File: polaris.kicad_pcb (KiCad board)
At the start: 4 copper layers, 170 parts, among them J1001 Conn_Coaxial, J101 XT60-M, J102 PYRO0, J103 PYRO1, J104 PYRO2, J105 PYRO3, J106 PYRO4, J107 PYRO5, J108 SERVO0, J109 SERVO1, J110 SERVO2, J111 SERVO3, J112 SERVO4, J113 SERVO5, J114 SPI, J115 I2C, J116 PB, J117 SWD, J301 USB_C_Receptacle_USB2.0_16P, J401 GNSS, J501 XT60-M, Q201 IRLZ44N, Q202 IRLZ44N, Q401 Q_NMOS, Q501 IRLZ44N, Q502 IRLZ44N, Q503 IRLZ44N, Q504 IRLZ44N, Q505 IRLZ44N, Q506 IRLZ44N, SW401 SW_Push, SW402 SW_Push, U1001 Ra-08H, U1101 THD-2528-11SD-GF, U1201 W25Q128JVE, U201 BQ24005, U202 LM74700, U203 LM74700, U204 TLV75733PDBV, U205 LMR51430, U206 TPS7A2033PDBVR, U301 USBLC6-2SC6, U302 CH224K, U303 USBLC6-2SC6, U403 STM32F446VETx, U501 PC817, U502 PC817, U503 PC817, U504 PC817, U505 PC817, U506 PC817, U507 CD4051B, U601 ICM-42688-P, U701 LSM6DSO32TR, U801 MS5607, U901 LPS22HH, Y401 YXC YSX321SL

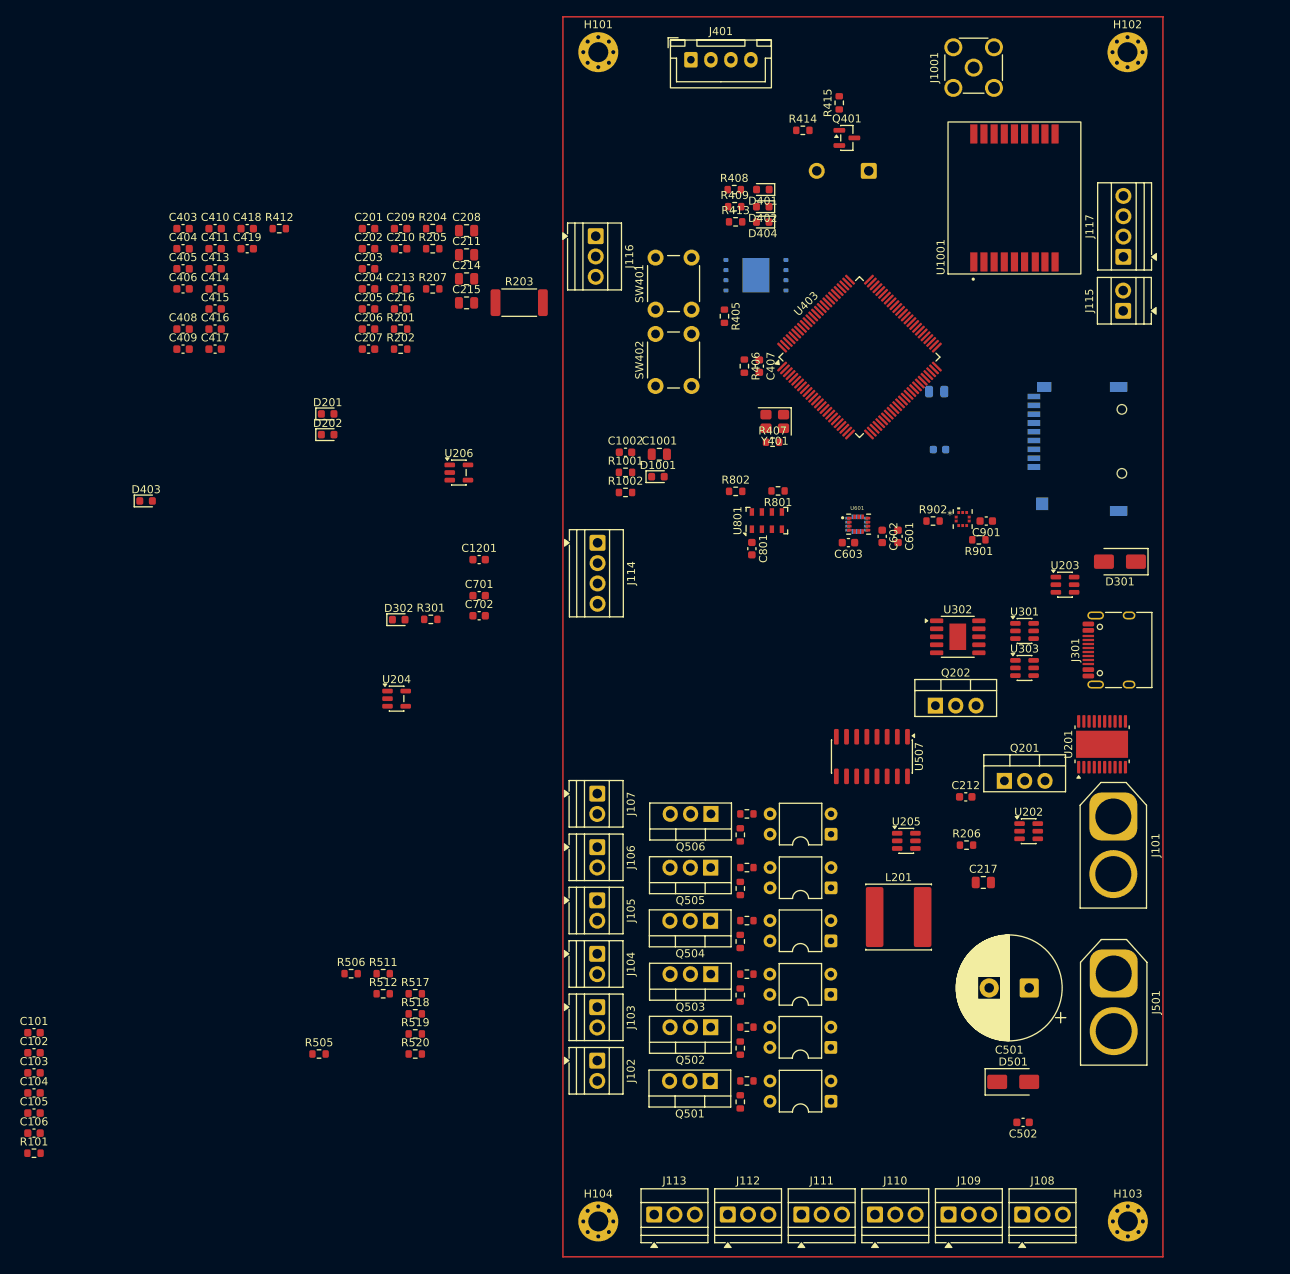
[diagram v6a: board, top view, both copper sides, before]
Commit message: Continued rough component placement
Finished most of component placement, only a few passives remain
Board dimensions basically locked at 155x75 mm
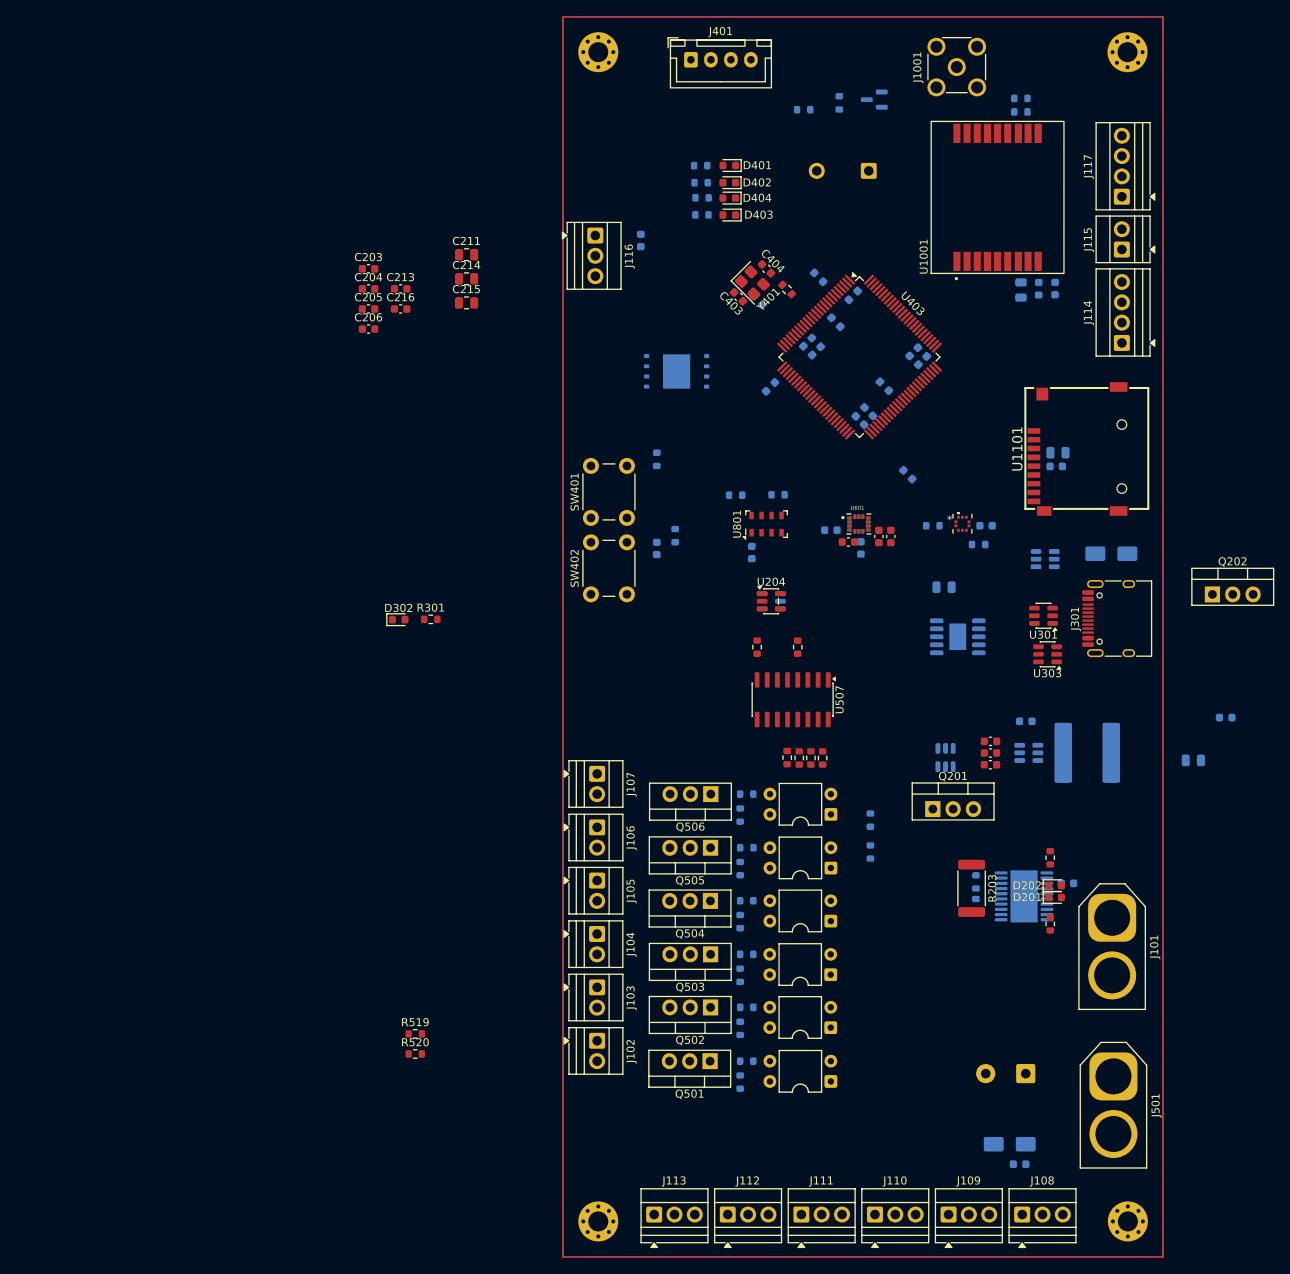
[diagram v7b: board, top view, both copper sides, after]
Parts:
- removed C101, C102, C103, C104, C105, C106: 100n, Capacitor_SMD:C_0603_1608Metric
- removed R101: 0R, Resistor_SMD:R_0603_1608Metric
- C1001, C1002, C1201, C201, C202, C208, C212, C217, C405, C406, C407, C408, C409, C410, C411, C413, C414, C415, C416, C417, C418, C419, C501, C701, C702, C801, C901, D1001, D301, D501, L201, Q401, R1001, R1002, R201, R202, R206, R207, R405, R406, R408, R409, R412, R413, R414, R415, R501, R502, R503, R504, R507, R508, R509, R510, R513, R514, R515, R516, R801, R802, R901, R902, U201, U202, U203, U205, U206, U302: moved to B.Cu
- C502: value C -> 4u7; moved to B.Cu
- U1101: moved to F.Cu
- moved C201 123.3 mm to (169.8, 112.6)
- moved C202 118.0 mm to (150.1, 133.3)
- moved R205 114.4 mm to (147.9, 138.4), turned to -90 degrees
- moved R204 110.2 mm to (147.9, 130.1), turned to 90 degrees
- moved D201 109.2 mm to (148.5, 135.1)
- moved D202 107.0 mm to (148.5, 133.6)
- moved R202 100.1 mm to (138.6, 136.1), turned to -90 degrees
- moved R201 99.7 mm to (138.6, 133.1), turned to -90 degrees
- moved C209 97.7 mm to (140.4, 115.6), turned to 180 degrees
- moved C210 97.0 mm to (140.4, 117.0), turned to 180 degrees
- moved C207 93.5 mm to (140.4, 118.5), turned to 180 degrees
- moved R203 92.5 mm to (138.1, 133.9), turned to -90 degrees
- moved C410 91.9 mm to (130.1, 82.2), turned to -45 degrees
- moved C409 91.4 mm to (130.9, 67.9), turned to 135 degrees
- moved C413 89.0 mm to (131.9, 66.9), turned to 135 degrees
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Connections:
- C405 pad 1: Net-(U403-VREF+) -> +3.3V
- C406 pad 1: Net-(U403-VREF+) -> +3.3V
- C501 pad 2: GND1 -> GND
- C502 pad 2: GND1 -> GND
- D501 pad 1: GND1 -> GND
- J108 pad 3: GND1 -> GND
- J109 pad 3: GND1 -> GND
- J110 pad 3: GND1 -> GND
- J111 pad 3: GND1 -> GND
- J112 pad 3: GND1 -> GND
- J113 pad 3: GND1 -> GND
- U403 pad 21: Net-(U403-VREF+) -> +3.3V
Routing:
- removed copper zone on In1.Cu, net GND
- removed copper zone on In2.Cu, net GND

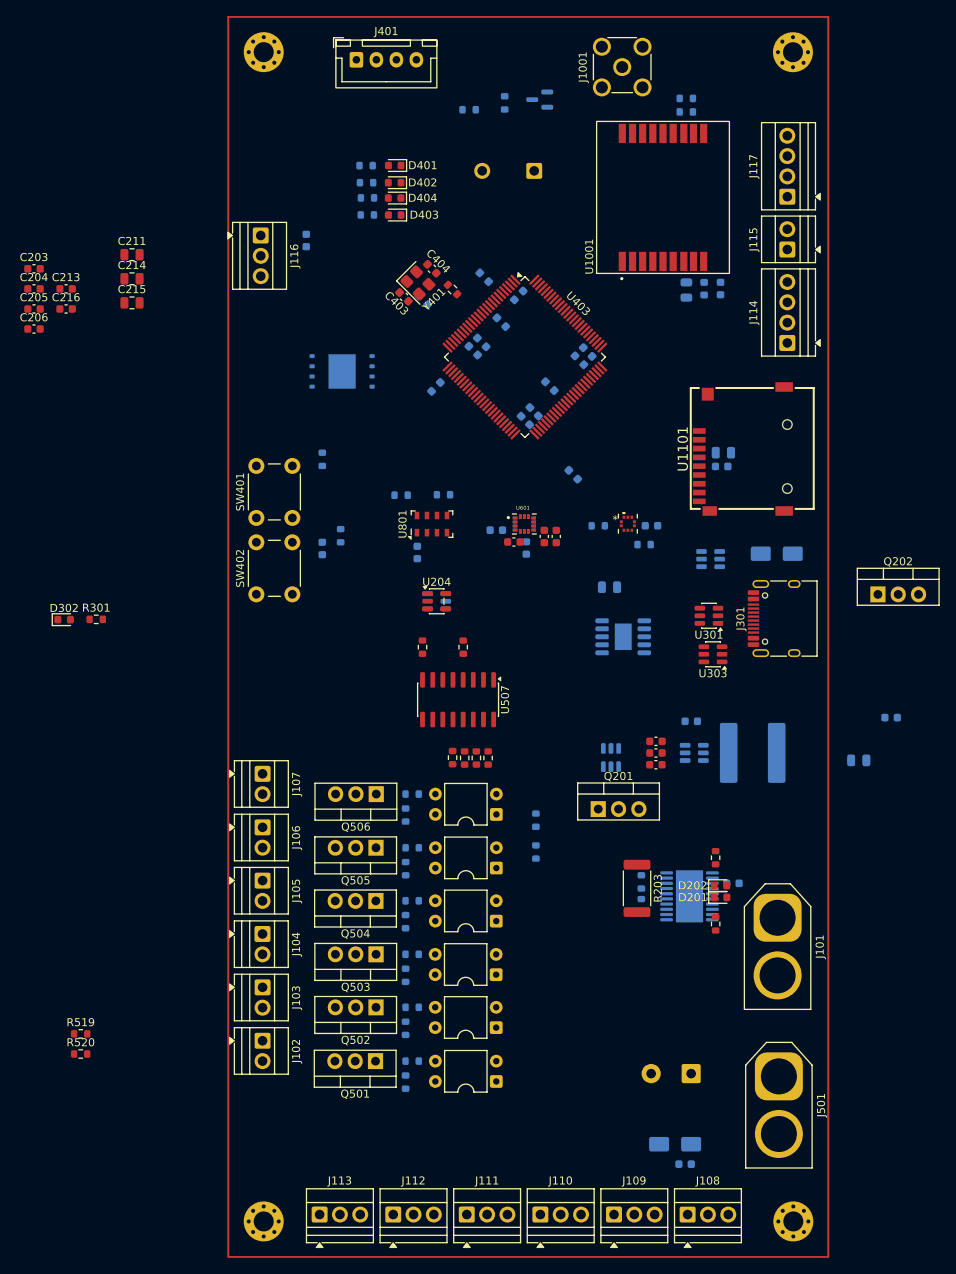
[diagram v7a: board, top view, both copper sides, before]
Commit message: Completed rough component placement
Began laying out traces
Small change to page 12 of schematic (FLASH):
Connected exposed pad to GND (not sure why I didn't connect it previously)
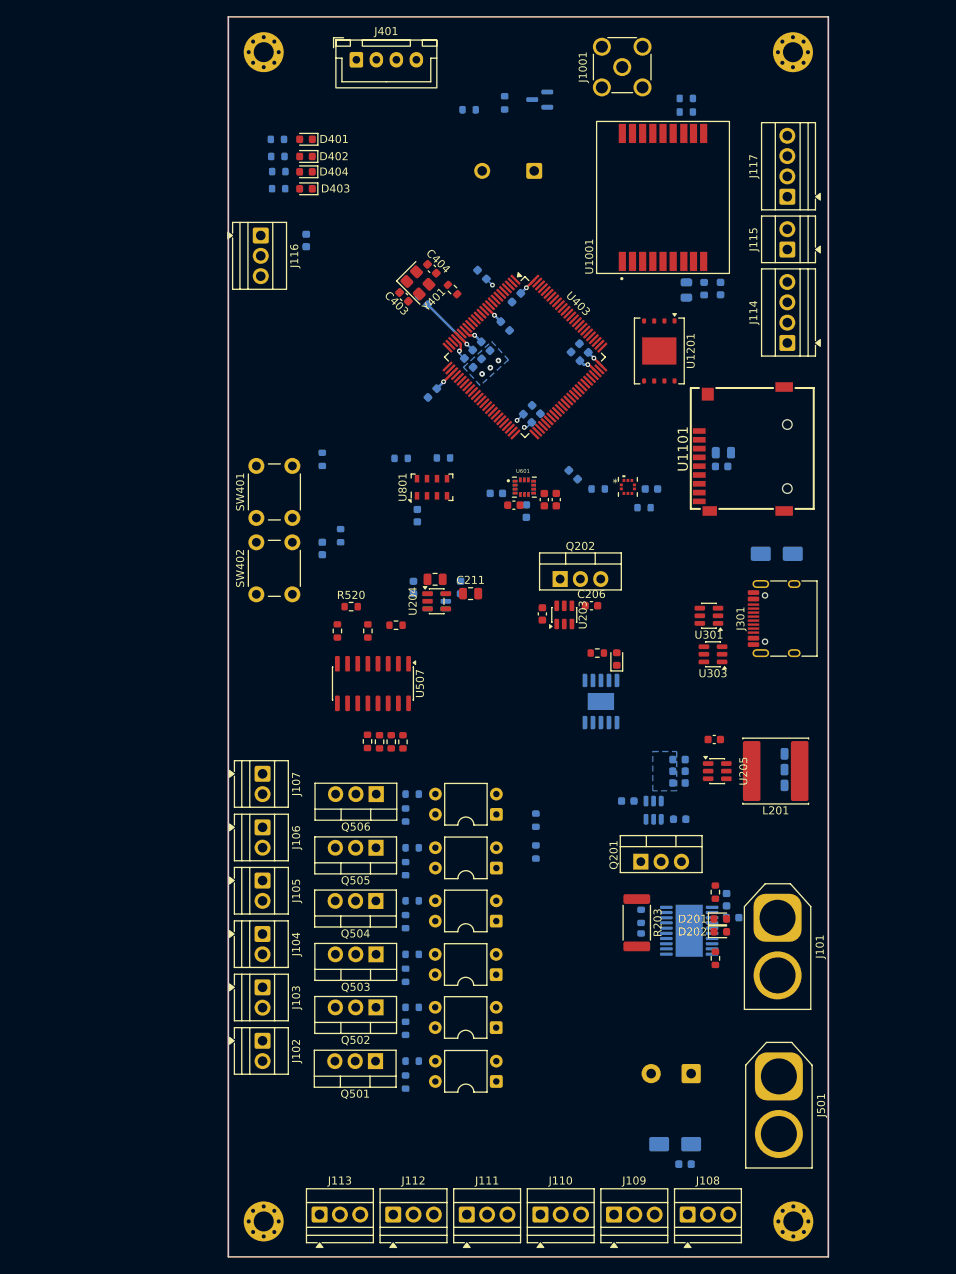
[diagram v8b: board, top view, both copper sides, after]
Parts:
- C203, C205, C207, C209, C210, C213, C214, C215, C216: moved to B.Cu
- C208, C212, L201, U1201, U203, U205: moved to F.Cu
- moved C205 102.9 mm to (143.4, 125.3)
- moved C214 101.7 mm to (157.5, 117.1)
- moved C215 101.1 mm to (157.5, 119.1)
- moved C203 99.7 mm to (136.9, 123.0)
- moved C206 77.8 mm to (132.4, 98.6)
- moved C204 75.4 mm to (126.2, 99.6), turned to -90 degrees
- moved D302 69.3 mm to (135.6, 105.3), turned to 90 degrees
- moved R520 65.3 mm to (102.3, 98.7)
- moved R519 64.5 mm to (108.0, 101.0)
- moved R301 62.8 mm to (133.1, 104.5)
- moved C213 61.8 mm to (116.0, 96.3), turned to 90 degrees
- moved C211 59.9 mm to (117.3, 97.1)
- moved C216 55.7 mm to (110.1, 96.3), turned to 90 degrees
- moved Q202 39.8 mm to (128.5, 95.3)
- moved U1201 39.7 mm to (140.9, 66.8), turned to -90 degrees
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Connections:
- U1201 pad 9: unconnected-(U1201-EP-Pad9) -> GND
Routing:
- net +3.3V: track 0.00 -> 27.6 mm, vias 0 -> 9
- net Net-(U403-VCAP_2): track 0.00 -> 2.69 mm, vias 0 -> 1
- net Net-(U403-VCAP_1): track 0.00 -> 1.11 mm, vias 0 -> 1
- net GND: vias 0 -> 3
- added copper zone on B.Cu, net (none)
- added copper zone on B.Cu, net GND
- added copper zone on In1.Cu, net GND
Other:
- board outline added: 75 x 155 mm
